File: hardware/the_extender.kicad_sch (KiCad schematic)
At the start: 117 parts, among them J0 U262-241N-4BV60, J1 USB_C_Receptacle_USB2.0, J2 U231-091N-3BLRC11, J3 PJ-3136-B, J4 PJ-3136-B, J5 AF 10.0 HC6.3, Q1 SSM3J332R,LF, Q2 SSM3J332R,LF, Q3 Q_PNP_CBE, Q4 SSM3J332R,LF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

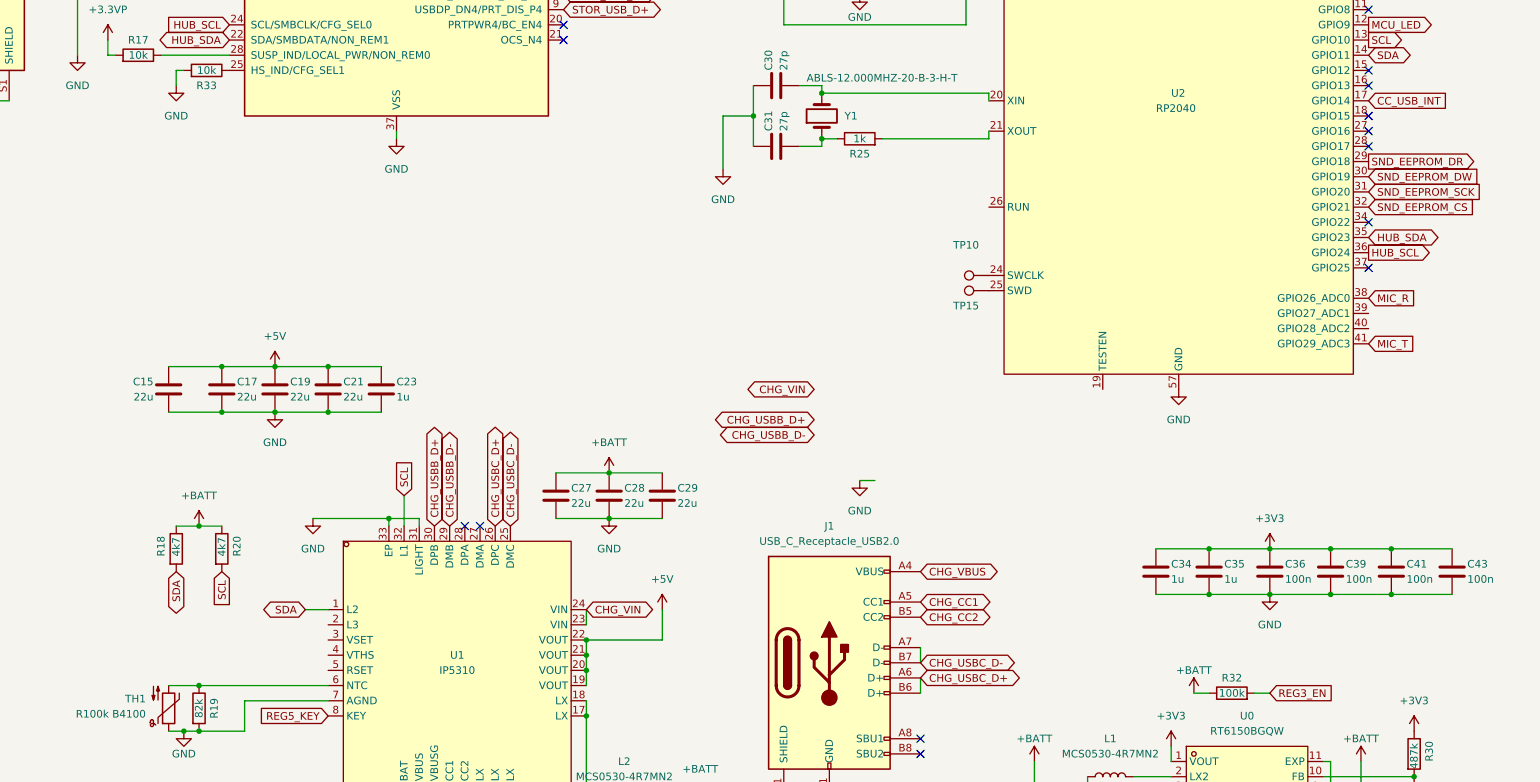
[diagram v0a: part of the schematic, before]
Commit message: added some missing connections
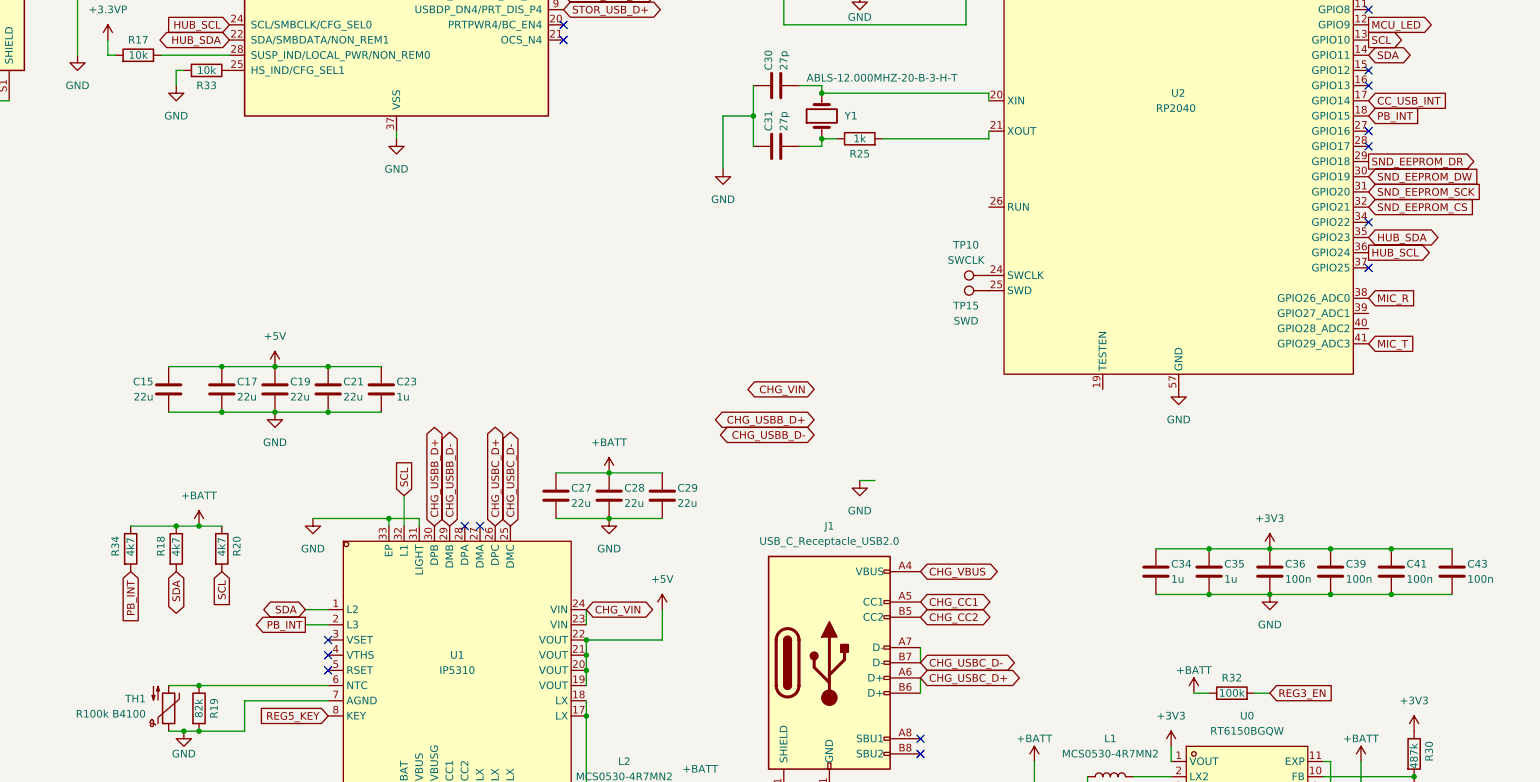
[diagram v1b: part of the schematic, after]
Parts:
- added R34: 4k7, Resistor_SMD:R_0805_2012Metric_Pad1.20x1.40mm_HandSolder, symbol Device:R
- TP10: value (none) -> SWCLK
- TP15: value (none) -> SWD
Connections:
- net +BATT: now also R34.1
- net PB_INT: now reaches U2.18 (GPIO15)
- net PB_INT: now also U1.2 (L3), R34.2
- no-connect marks 50 -> 52
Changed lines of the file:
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@@
   (junction (at 243.84 200.66) (diameter 0) (color 0 0 0 0)
   )
+  (junction (at 175.26 181.61) (diameter 0) (color 0 0 0 0)
+  )
   (junction (at 327.66 57.15) (diameter 0) (color 0 0 0 0)
   )
@@
   (no_connect (at 240.03 72.39))
   (no_connect (at 240.03 62.23))
+  (no_connect (at 200.66 200.66))
+  (no_connect (at 200.66 203.2))
+  (no_connect (at 200.66 205.74))
   (no_connect (at 184.15 69.85))
   (no_connect (at 374.65 80.01))
@@
   (no_connect (at 80.01 163.83))
   (no_connect (at 374.65 118.11))
-  (no_connect (at 374.65 113.03))
   (no_connect (at 39.37 161.29))
   (no_connect (at 55.88 193.04))
@@
     (stroke (width 0) (type default) (color 0 0 0 0))
   )
+  (wire (pts (xy 196.85 198.12) (xy 200.66 198.12))
+    (stroke (width 0) (type default) (color 0 0 0 0))
+  )
   (wire (pts (xy 33.02 166.37) (xy 39.37 166.37))
     (stroke (width 0) (type default) (color 0 0 0 0))
@@
     (stroke (width 0) (type default) (color 0 0 0 0))
   )
+  (wire (pts (xy 167.64 181.61) (xy 175.26 181.61))
+    (stroke (width 0) (type default) (color 0 0 0 0))
+  )
   (wire (pts (xy 99.06 77.47) (xy 124.46 77.47))
     (stroke (width 0) (type default) (color 0 0 0 0))
@@
     )
   )
+  (global_label "PB_INT" (shape input) (at 374.65 113.03 0) (fields_autoplaced)
+    (effects (font (size 1.27 1.27)) (justify left))
+    (property "Intersheet References" "${INTERSHEET_REFS}" (id 0) (at 383.4736 112.9506 0)
+      (effects (font (size 1.27 1.27)) (justify left) hide)
+    )
+  )
   (global_label "CC1" (shape tri_state) (at 306.07 17.78 270) (fields_autoplaced)
     (effects (font (size 1.27 1.27)) (justify right))
@@
     )
   )
+  (global_label "PB_INT" (shape output) (at 196.85 198.12 180) (fields_autoplaced)
+    (effects (font (size 1.27 1.27)) (justify right))
+    (property "Intersheet References" "${INTERSHEET_REFS}" (id 0) (at 188.0264 198.0406 0)
+      (effects (font (size 1.27 1.27)) (justify right) hide)
+    )
+  )
   (global_label "HOST_USB_D+" (shape bidirectional) (at 184.15 62.23 180) (fields_autoplaced)
     (effects (font (size 1.27 1.27)) (justify right))
@@
     )
   )
+  (global_label "PB_INT" (shape input) (at 167.64 189.23 270) (fields_autoplaced)
+    (effects (font (size 1.27 1.27)) (justify right))
+    (property "Intersheet References" "${INTERSHEET_REFS}" (id 0) (at 167.5606 198.0536 90)
+      (effects (font (size 1.27 1.27)) (justify right) hide)
+    )
+  )
   (global_label "MCU_LED" (shape input) (at 74.93 212.09 90) (fields_autoplaced)
     (effects (font (size 1.27 1.27)) (justify left))
@@
     (in_bom yes) (on_board yes)
     (property "Reference" "TP15" (id 0) (at 307.34 144.78 90))
-    (property "Value" "" (id 1) (at 307.34 147.32 90))
+    (property "Value" "SWD" (id 1) (at 307.34 147.32 90))
     (property "Footprint" "TestPoint:TestPoint_Pad_D2.0mm" (id 2) (at 311.15 137.16 0)
       (effects (font (size 1.27 1.27)) hide)
@@
     (in_bom yes) (on_board yes)
     (property "Reference" "TP10" (id 0) (at 307.34 134.62 90))
-    (property "Value" "" (id 1) (at 307.34 137.16 90))
+    (property "Value" "SWCLK" (id 1) (at 307.34 137.16 90))
     (property "Footprint" "TestPoint:TestPoint_Pad_D2.0mm" (id 2) (at 311.15 134.62 0)
       (effects (font (size 1.27 1.27)) hide)
@@
     (pin "1")
   )
+  (symbol (lib_id "Device:R") (at 167.64 185.42 0) (unit 1)
+    (in_bom yes) (on_board yes)
+    (property "Reference" "R34" (id 0) (at 165.1 186.69 90)
+      (effects (font (size 1.27 1.27)) (justify left))
+    )
+    (property "Value" "4k7" (id 1) (at 167.64 186.69 90)
+      (effects (font (size 1.27 1.27)) (justify left))
+    )
+    (property "Footprint" "Resistor_SMD:R_0805_2012Metric_Pad1.20x1.40mm_HandSolder" (id 2) (at 165.862 185.42 90)
+      (effects (font (size 1.27 1.27)) hide)
+    )
+    (property "Datasheet" "~" (id 3) (at 167.64 185.42 0)
+      (effects (font (size 1.27 1.27)) hide)
+    )
+    (pin "1")
+    (pin "2")
+  )
   (symbol (lib_id "Device:R") (at 381 67.31 90) (unit 1)
     (in_bom yes) (on_board yes)
@@
       (reference "R33") (unit 1) (value "10k") (footprint "Resistor_SMD:R_0805_2012Metric_Pad1.20x1.40mm_HandSolder")
     )
+    (path "/e6e84f42-dc69-4e44-9e0c-06d99eedd7ef"
+      (reference "R34") (unit 1) (value "4k7") (footprint "Resistor_SMD:R_0805_2012Metric_Pad1.20x1.40mm_HandSolder")
+    )
     (path "/67800f9e-414e-49be-af4c-0f14dddef3de"

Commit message: fix bugs
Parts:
- added C9: 1u, Capacitor_SMD:C_0805_2012Metric_Pad1.18x1.45mm_HandSolder, symbol Device:C
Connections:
- net GND: now also C9.2
- net at U6.39 (AREG36): now also C9.1
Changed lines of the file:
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@@
     (pin "1")
+  )
+  (symbol (lib_id "Device:C") (at 73.66 133.35 90) (unit 1)
+    (in_bom yes) (on_board yes)
+    (property "Reference" "C9" (id 0) (at 72.39 130.81 0)
+      (effects (font (size 1.27 1.27)) (justify left))
+    )
+    (property "Value" "1u" (id 1) (at 74.93 130.81 0)
+      (effects (font (size 1.27 1.27)) (justify left))
+    )
+    (property "Footprint" "Capacitor_SMD:C_0805_2012Metric_Pad1.18x1.45mm_HandSolder" (id 2) (at 77.47 132.3848 0)
+      (effects (font (size 1.27 1.27)) hide)
+    )
+    (property "Datasheet" "~" (id 3) (at 73.66 133.35 0)
+      (effects (font (size 1.27 1.27)) hide)
+    )
+    (pin "1")
+    (pin "2")
   )
   (symbol (lib_id "Connector:USB_C_Receptacle_USB2.0") (at 284.48 204.47 0) (unit 1)
@@
       (reference "C8") (unit 1) (value "100n") (footprint "Capacitor_SMD:C_0805_2012Metric_Pad1.18x1.45mm_HandSolder")
     )
+    (path "/969ca741-ce84-4255-8947-4da4ccf7f630"
+      (reference "C9") (unit 1) (value "1u") (footprint "Capacitor_SMD:C_0805_2012Metric_Pad1.18x1.45mm_HandSolder")
+    )
     (path "/d89905a7-5f72-4d61-9664-b9353d028220"

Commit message: use default footprints
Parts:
- U0: value RT6150BGQW -> (none); footprint easyeda2kicad:WSON-10_L2.5-W2.5-P0.50-BL-EP -> (none)
- U1: value IP5310 -> (none); footprint easyeda2kicad:QFN-32_L5.0-W5.0-P0.50-BL-EP3.4 -> (none)
- U6: value HS-100B -> (none); footprint easyeda2kicad:LQFP-48_L7.0-W7.0-P0.50-LS9.0-BL -> (none)
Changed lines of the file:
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@@
     (in_bom yes) (on_board yes)
     (property "Reference" "U1" (id 0) (at 222.25 203.2 0))
-    (property "Value" "IP5310" (id 1) (at 222.25 205.74 0))
-    (property "Footprint" "easyeda2kicad:QFN-32_L5.0-W5.0-P0.50-BL-EP3.4" (id 2) (at 222.25 234.95 0)
+    (property "Value" "" (id 1) (at 222.25 205.74 0))
+    (property "Footprint" "" (id 2) (at 222.25 234.95 0)
       (effects (font (size 1.27 1.27)) hide)
     )
@@
   )
   (symbol (lib_id "LCSC:HS-100B") (at 59.69 165.1 0) (unit 1)
-    (in_bom yes) (on_board yes)
+    (in_bom yes) (on_board no)
     (property "Reference" "U6" (id 0) (at 59.69 163.83 0))
-    (property "Value" "HS-100B" (id 1) (at 59.69 166.37 0))
-    (property "Footprint" "easyeda2kicad:LQFP-48_L7.0-W7.0-P0.50-LS9.0-BL" (id 2) (at 59.69 200.66 0)
+    (property "Value" "" (id 1) (at 59.69 166.37 0))
+    (property "Footprint" "" (id 2) (at 59.69 200.66 0)
       (effects (font (size 1.27 1.27)) hide)
     )
@@
     (in_bom yes) (on_board yes)
     (property "Reference" "U0" (id 0) (at 354.33 213.36 0))
-    (property "Value" "RT6150BGQW" (id 1) (at 354.33 215.9 0))
-    (property "Footprint" "easyeda2kicad:WSON-10_L2.5-W2.5-P0.50-BL-EP" (id 2) (at 354.33 241.3 0)
+    (property "Value" "" (id 1) (at 354.33 215.9 0))
+    (property "Footprint" "" (id 2) (at 354.33 241.3 0)
       (effects (font (size 1.27 1.27)) hide)
     )
@@
     )
     (path "/ba2366c8-9666-4a03-997b-de57f5e99126"
-      (reference "U0") (unit 1) (value "RT6150BGQW") (footprint "easyeda2kicad:WSON-10_L2.5-W2.5-P0.50-BL-EP")
+      (reference "U0") (unit 1) (value "RT6150BGQW") (footprint "Package_SON:WSON-10-1EP_2.5x2.5mm_P0.5mm_EP1.2x2mm")
     )
     (path "/4ca92096-0499-4734-8620-6a654dac35e8"
-      (reference "U1") (unit 1) (value "IP5310") (footprint "easyeda2kicad:QFN-32_L5.0-W5.0-P0.50-BL-EP3.4")
+      (reference "U1") (unit 1) (value "IP5310") (footprint "Package_DFN_QFN:QFN-32-1EP_5x5mm_P0.5mm_EP3.45x3.45mm")
     )
     (path "/44fd8df2-cc1a-47a1-b6cc-08af9e746772"
@@
     )
     (path "/4e19351f-52c9-4675-8c17-fe1a9a3bf9d5"
-      (reference "U6") (unit 1) (value "HS-100B") (footprint "easyeda2kicad:LQFP-48_L7.0-W7.0-P0.50-LS9.0-BL")
+      (reference "U6") (unit 1) (value "HS-100B") (footprint "Package_QFP:LQFP-48_7x7mm_P0.5mm")
     )
     (path "/09aa4fee-b5e8-49f8-b7eb-59dbd608c6e0"

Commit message: add missing trace, fix bugs
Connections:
- net SND_MIC_EN: now also U2.34 (GPIO22)
- no-connect marks 52 -> 51
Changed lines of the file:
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@@
   (no_connect (at 374.65 82.55))
   (no_connect (at 184.15 82.55))
-  (no_connect (at 374.65 130.81))
   (no_connect (at 240.03 59.69))
   (no_connect (at 240.03 74.93))
@@
     )
   )
+  (global_label "SND_MIC_EN" (shape output) (at 374.65 130.81 0) (fields_autoplaced)
+    (effects (font (size 1.27 1.27)) (justify left))
+    (property "Intersheet References" "${INTERSHEET_REFS}" (id 0) (at 388.6141 130.7306 0)
+      (effects (font (size 1.27 1.27)) (justify left) hide)
+    )
+  )

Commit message: added even more connections i forgot
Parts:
- U0: value (none) -> RT6150BGQW; footprint (none) -> Package_SON:WSON-10-1EP_2.5x2.5mm_P0.5mm_EP1.2x2mm
- U1: value (none) -> IP5310; footprint (none) -> Package_DFN_QFN:QFN-32-1EP_5x5mm_P0.5mm_EP3.45x3.45mm
- U6: value (none) -> HS-100B; footprint (none) -> Package_QFP:LQFP-48_7x7mm_P0.5mm
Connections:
- net +3.3VP: now also U5.26 (RESET_N)
- net HUB_EN: now also U2.6 (GPIO4); no longer U2.3 (GPIO1)
- net REG3_PS: now also U2.7 (GPIO5)
- no-connect marks 51 -> 53
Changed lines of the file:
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@@
   (no_connect (at 374.65 90.17))
   (no_connect (at 374.65 115.57))
-  (no_connect (at 374.65 87.63))
   (no_connect (at 240.03 100.33))
   (no_connect (at 240.03 97.79))
@@
   (no_connect (at 299.72 219.71))
   (no_connect (at 374.65 138.43))
+  (no_connect (at 124.46 85.09))
   (no_connect (at 374.65 95.25))
   (no_connect (at 299.72 217.17))
-  (no_connect (at 374.65 92.71))
   (no_connect (at 124.46 100.33))
+  (no_connect (at 124.46 95.25))
   (no_connect (at 374.65 82.55))
   (no_connect (at 184.15 82.55))
@@
   (no_connect (at 184.15 69.85))
   (no_connect (at 374.65 80.01))
+  (no_connect (at 124.46 87.63))
   (no_connect (at 374.65 107.95))
   (no_connect (at 124.46 102.87))
-  (no_connect (at 374.65 85.09))
+  (no_connect (at 124.46 92.71))
   (no_connect (at 50.8 193.04))
   (no_connect (at 48.26 193.04))
@@
   (no_connect (at 80.01 163.83))
   (no_connect (at 374.65 118.11))
+  (no_connect (at 374.65 92.71))
   (no_connect (at 39.37 161.29))
   (no_connect (at 55.88 193.04))
@@
     (stroke (width 0) (type default) (color 0 0 0 0))
   )
+  (wire (pts (xy 162.56 67.31) (xy 184.15 67.31))
+    (stroke (width 0) (type default) (color 0 0 0 0))
+  )
   (wire (pts (xy 243.84 213.36) (xy 243.84 227.33))
     (stroke (width 0) (type default) (color 0 0 0 0))
@@
     (stroke (width 0) (type default) (color 0 0 0 0))
   )
+  (wire (pts (xy 162.56 66.04) (xy 162.56 67.31))
+    (stroke (width 0) (type default) (color 0 0 0 0))
+  )
   (wire (pts (xy 271.78 113.03) (xy 271.78 118.11))
     (stroke (width 0) (type default) (color 0 0 0 0))
@@
     )
   )
-  (global_label "HUB_EN" (shape output) (at 374.65 77.47 0) (fields_autoplaced)
+  (global_label "HUB_EN" (shape output) (at 374.65 85.09 0) (fields_autoplaced)
     (effects (font (size 1.27 1.27)) (justify left))
-    (property "Intersheet References" "${INTERSHEET_REFS}" (id 0) (at 384.4412 77.3906 0)
+    (property "Intersheet References" "${INTERSHEET_REFS}" (id 0) (at 384.4412 85.0106 0)
       (effects (font (size 1.27 1.27)) (justify left) hide)
     )
@@
     )
   )
-  (global_label "HUB_RESET" (shape input) (at 182.88 67.31 180) (fields_autoplaced)
-    (effects (font (size 1.27 1.27)) (justify right))
-    (property "Intersheet References" "${INTERSHEET_REFS}" (id 0) (at 169.8231 67.2306 0)
-      (effects (font (size 1.27 1.27)) (justify right) hide)
-    )
-  )
   (global_label "REG5_KEY" (shape input) (at 200.66 213.36 180) (fields_autoplaced)
     (effects (font (size 1.27 1.27)) (justify right))
@@
     )
   )
+  (global_label "REG3_PS" (shape output) (at 374.65 87.63 0) (fields_autoplaced)
+    (effects (font (size 1.27 1.27)) (justify left))
+    (property "Intersheet References" "${INTERSHEET_REFS}" (id 0) (at 385.4088 87.5506 0)
+      (effects (font (size 1.27 1.27)) (justify left) hide)
+    )
+  )
   (global_label "STOR_USB_D-" (shape bidirectional) (at 57.15 62.23 0) (fields_autoplaced)
     (effects (font (size 1.27 1.27)) (justify left))
@@
     (pin "1")
   )
+  (symbol (lib_id "power:+3.3VP") (at 162.56 66.04 0) (unit 1)
+    (in_bom yes) (on_board yes) (fields_autoplaced)
+    (property "Reference" "#PWR0112" (id 0) (at 166.37 67.31 0)
+      (effects (font (size 1.27 1.27)) hide)
+    )
+    (property "Value" "+3.3VP" (id 1) (at 162.56 60.96 0))
+    (property "Footprint" "" (id 2) (at 162.56 66.04 0)
+      (effects (font (size 1.27 1.27)) hide)
+    )
+    (property "Datasheet" "" (id 3) (at 162.56 66.04 0)
+      (effects (font (size 1.27 1.27)) hide)
+    )
+    (pin "1")
+  )
   (symbol (lib_id "power:GNDA") (at 83.82 186.69 0) (unit 1)
     (in_bom yes) (on_board yes) (fields_autoplaced)
@@
     (in_bom yes) (on_board yes)
     (property "Reference" "U1" (id 0) (at 222.25 203.2 0))
-    (property "Value" "" (id 1) (at 222.25 205.74 0))
-    (property "Footprint" "" (id 2) (at 222.25 234.95 0)
+    (property "Value" "IP5310" (id 1) (at 222.25 205.74 0))
+    (property "Footprint" "Package_DFN_QFN:QFN-32-1EP_5x5mm_P0.5mm_EP3.45x3.45mm" (id 2) (at 222.25 234.95 0)
       (effects (font (size 1.27 1.27)) hide)
     )
@@
     (in_bom yes) (on_board no)
     (property "Reference" "U6" (id 0) (at 59.69 163.83 0))
-    (property "Value" "" (id 1) (at 59.69 166.37 0))
-    (property "Footprint" "" (id 2) (at 59.69 200.66 0)
+    (property "Value" "HS-100B" (id 1) (at 59.69 166.37 0))
+    (property "Footprint" "Package_QFP:LQFP-48_7x7mm_P0.5mm" (id 2) (at 59.69 200.66 0)
       (effects (font (size 1.27 1.27)) hide)
     )
@@
     (in_bom yes) (on_board yes)
     (property "Reference" "U0" (id 0) (at 354.33 213.36 0))
-    (property "Value" "" (id 1) (at 354.33 215.9 0))
-    (property "Footprint" "" (id 2) (at 354.33 241.3 0)
+    (property "Value" "RT6150BGQW" (id 1) (at 354.33 215.9 0))
+    (property "Footprint" "Package_SON:WSON-10-1EP_2.5x2.5mm_P0.5mm_EP1.2x2mm" (id 2) (at 354.33 241.3 0)
       (effects (font (size 1.27 1.27)) hide)
     )
@@
       (reference "#PWR0111") (unit 1) (value "+5VA") (footprint "")
     )
+    (path "/351450a8-d1bf-47eb-ab4a-aa5c0db224b2"
+      (reference "#PWR0112") (unit 1) (value "+3.3VP") (footprint "")
+    )
     (path "/a5a0aa7d-b4f7-4e4a-affe-f90b7fc94626"

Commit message: fix
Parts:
- U6: value HS-100B -> (none); footprint Package_QFP:LQFP-48_7x7mm_P0.5mm -> (none)
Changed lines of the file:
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@@
     (in_bom yes) (on_board no)
     (property "Reference" "U6" (id 0) (at 59.69 163.83 0))
-    (property "Value" "HS-100B" (id 1) (at 59.69 166.37 0))
-    (property "Footprint" "Package_QFP:LQFP-48_7x7mm_P0.5mm" (id 2) (at 59.69 200.66 0)
+    (property "Value" "" (id 1) (at 59.69 166.37 0))
+    (property "Footprint" "" (id 2) (at 59.69 200.66 0)
       (effects (font (size 1.27 1.27)) hide)
     )
